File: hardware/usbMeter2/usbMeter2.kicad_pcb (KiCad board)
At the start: 2 copper layers, 17.5 x 50 mm, 50 parts, among them J1 USB_A, J2 USB_A, J3 USB_C_Receptacle_USB2.0_16P, SW1 SW_Push, SW2 SW_Push, SW3 SW_Push, U1 STM32G031G8Ux, U2 TPD4E05U06DQA, U3 TPD4E05U06DQA, U4 CH340E, U5 INA228, U6 CH217K, U7 RT9193-33GB

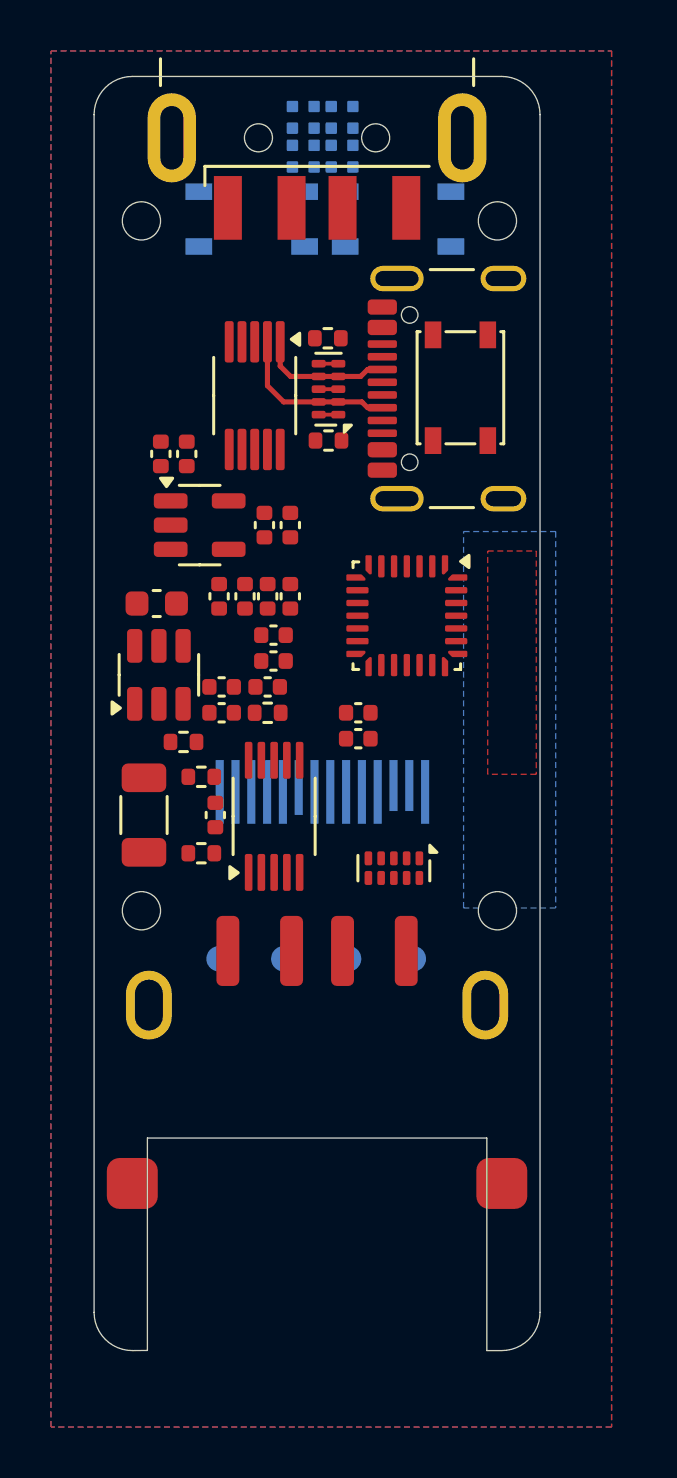
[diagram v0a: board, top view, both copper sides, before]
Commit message: usbmeter2尝试缩减了本体的尺寸，采用dcdc+ldo供电避免typea可能存在的高压输入
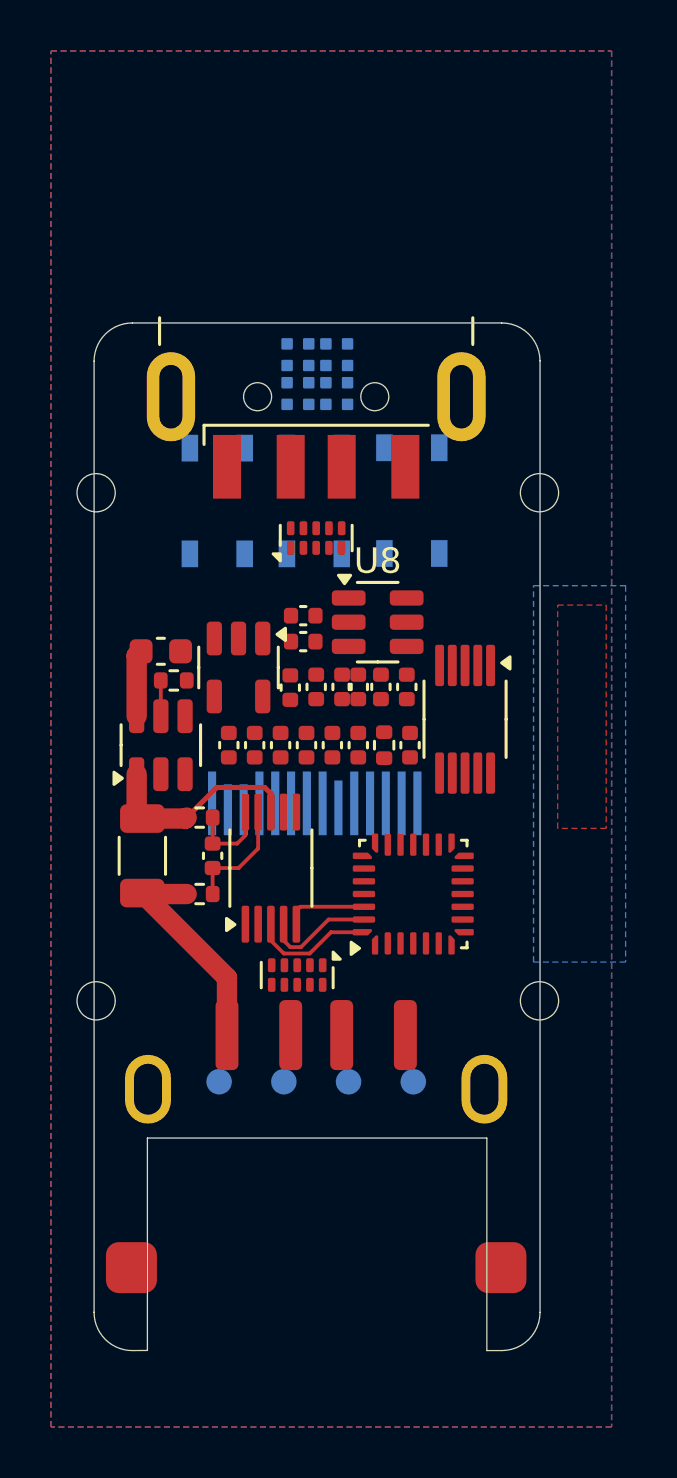
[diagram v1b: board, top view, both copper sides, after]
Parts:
- removed J3: USB_C_Receptacle_USB2.0_16P, Connector_USB:USB_C_Receptacle_GCT_USB4105-xx-A_16P_TopMnt_Horizontal
- removed R1, R2: 5.1k, Resistor_SMD:R_0402_1005Metric
- added U8: TPS54202DDC, Package_TO_SOT_SMD:SOT-23-6, F.Cu at (111.4, 88.6)
- SW3: moved to B.Cu
- moved U4 15.1 mm to (114.8, 92.5)
- moved SW1 13.1 mm to (105.2, 83.9), turned to -90 degrees
- moved SW2 12.6 mm to (112.6, 83.8), turned to 90 degrees
- moved U9 12.3 mm to (108.9, 101.7), turned to 0 degrees
- moved U1 10.9 mm to (112.8, 99.3), turned to 90 degrees
- moved H1 10.8 mm to (100.3, 83.6)
- moved H2 10.8 mm to (117.7, 83.6)
- moved J1 10.2 mm to (109.0, 72.9)
- moved D1 9.32 mm to (108.2, 79.7)
- moved D2 9.32 mm to (108.2, 78.1)
- moved D3 9.32 mm to (109.8, 78.1)
- moved D4 9.32 mm to (109.8, 79.7)
- moved C8 8.67 mm to (108.5, 89.4), turned to 0 degrees
- moved C7 8.46 mm to (108.5, 88.4), turned to 0 degrees
- moved C3 8.18 mm to (112.5, 91.2), turned to 90 degrees
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- renumbered C11 to C16, C12 to C17, C13 to C18, C14 to C19, C15 to C20, C16 to C21, C17 to C22, R7 to R12, U8 to U9
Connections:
- C7 pad 1: VBUS -> +5V
- C8 pad 1: VBUS -> +5V
- J1 pad 2: /D- -> /D2-
- J1 pad 3: /D+ -> /D2+
- J2 pad 1: +5V -> VBUS2
- R4 pad 2: +5V -> VBUS2
- R5 pad 1: +5V -> VBUS2
- U1 pad 17: /~{INA226_ALERT} -> unconnected-(U1-PC6-Pad17)
- U1 pad 26: /SCL -> /SCL1
- U1 pad 27: /SDA -> /SDA1
- U1 pad 28: unconnected-(U1-PB8-Pad28) -> /~{INA226_ALERT}
- U5 pad 4: /SDA2 -> /SDA1
- U5 pad 5: /SCL2 -> /SCL1
- U7 pad 1: VBUS -> +5V
- U7 pad 3: VBUS -> +5V
- U9 pad 10: /SCL -> /SCL2
- U9 pad 11: /SDA -> /SDA2
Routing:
- net VBUS2: track 0.00 -> 8.70 mm
- net /ch217x/VOUT: track 0.00 -> 8.21 mm
- net /D2-: track 6.59 -> 0.00 mm
- net /D2+: track 5.24 -> 0.00 mm
- net /~{INA226_ALERT}: track 0.00 -> 4.79 mm
- net Net-(U5-Vin-): track 0.00 -> 4.55 mm
- net /SDA1: track 0.00 -> 4.35 mm
- net Net-(U5-Vin+): track 0.00 -> 3.35 mm
- net /SCL1: track 0.00 -> 3.25 mm
- net VBUS: track 0.00 -> 2.62 mm
- net Net-(U6-ISET): track 0.00 -> 1.40 mm
- net Net-(U3-D2-): track 0.77 -> 0.00 mm
- net Net-(U3-D1+): track 0.77 -> 0.00 mm
- net GND: track 0.77 -> 0.00 mm
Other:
- board size 17.5 x 50 mm -> 17.5 x 40.3 mm
